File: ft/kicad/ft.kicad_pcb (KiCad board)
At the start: 2 copper layers, 21 x 33 mm, 2 parts, among them J1 Conn_RIOT, J2 Conn_ft

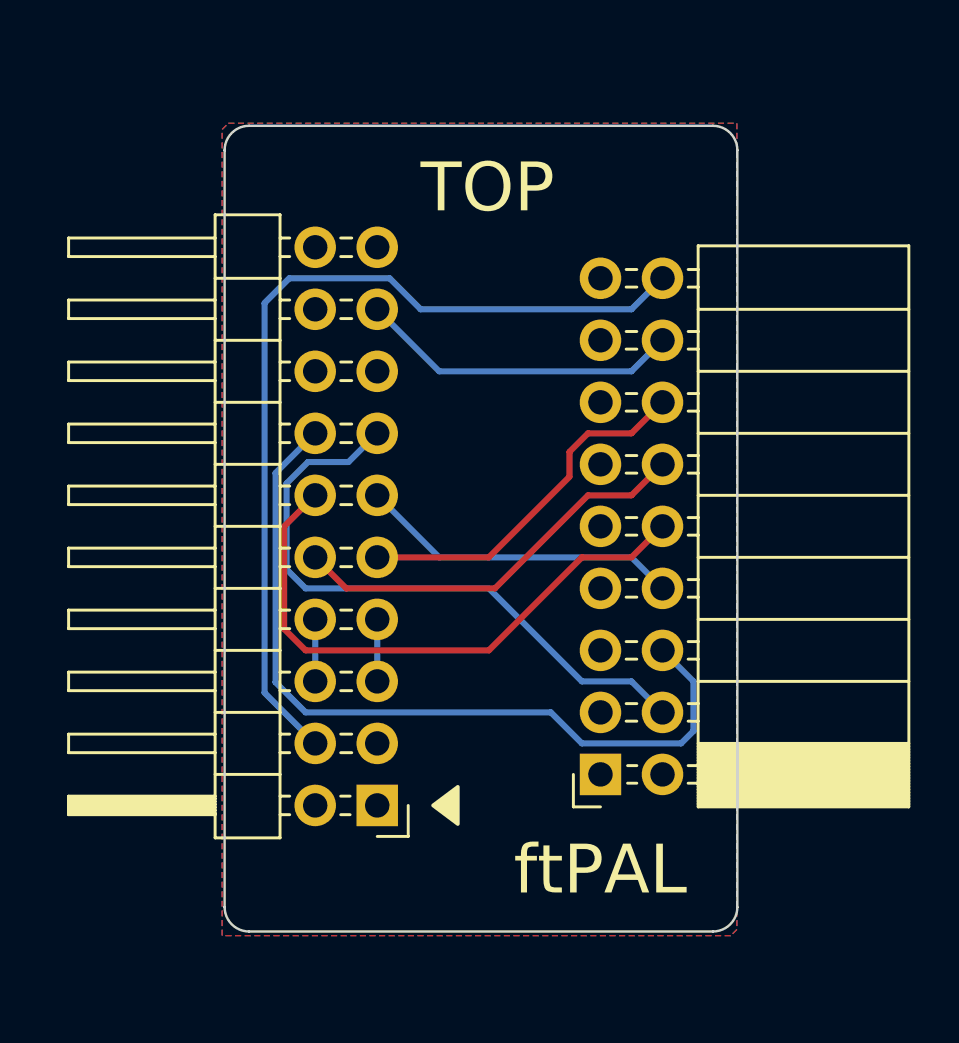
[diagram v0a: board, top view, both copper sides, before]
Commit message: Change ft interface connector to IDC type
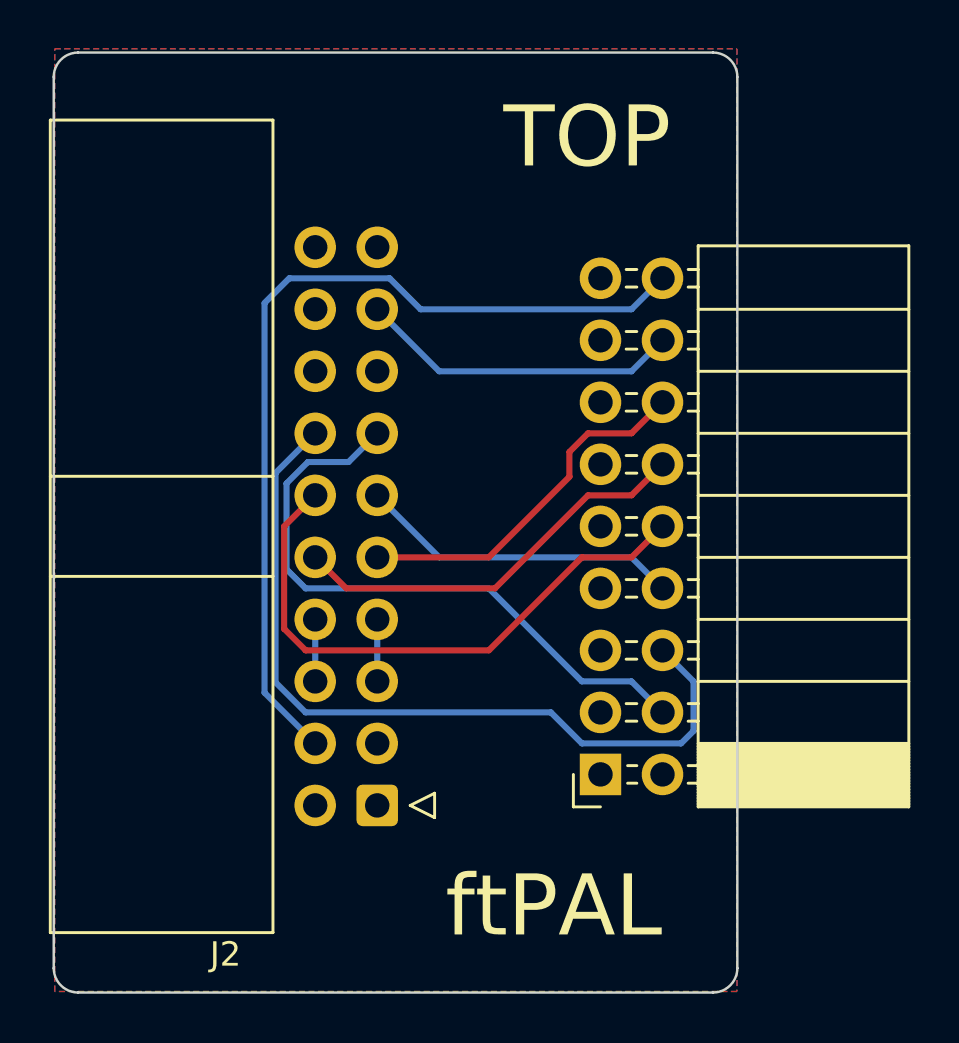
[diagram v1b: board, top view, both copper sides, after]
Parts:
- J2: footprint Connector_PinHeader_2.54mm:PinHeader_2x10_P2.54mm_Horizontal -> Connector_IDC:IDC-Header_2x10_P2.54mm_Horizontal
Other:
- board size 21 x 33 mm -> 28 x 38.5 mm
- board text added: "Plastic Objects Limited 2025"
- board text removed: "2025"
- board text removed: "Plastic Objects Limited"
